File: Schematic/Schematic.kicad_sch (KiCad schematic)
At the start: 2 parts, among them U1 NRF52840-DONGLE

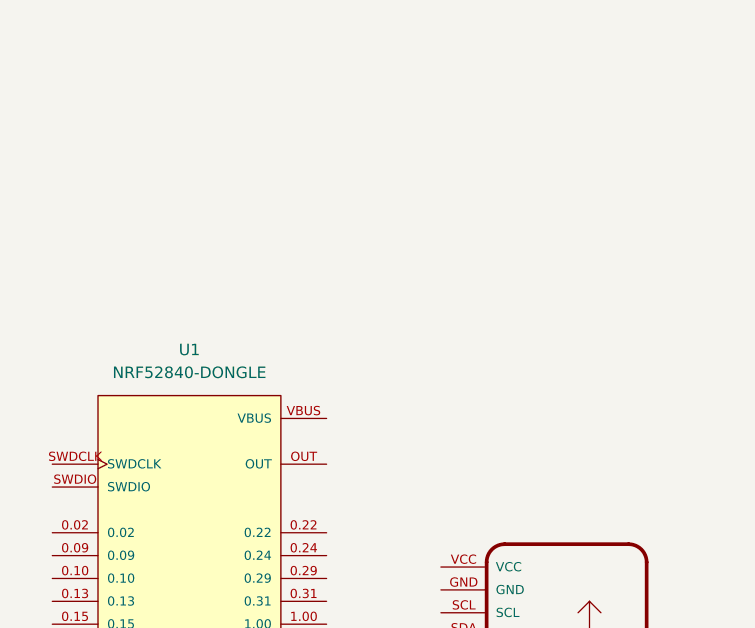
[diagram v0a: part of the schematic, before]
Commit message: PCB: adding the required symbols, footprints and 3D models
- create generic paths to the symbos and footprints, so there is no problem with setup on the other machine
- adding further PCB elements of the project
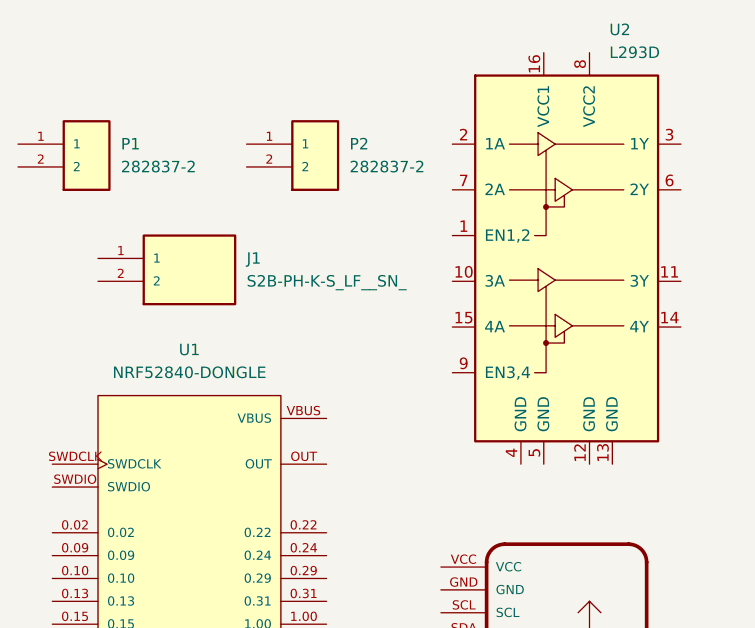
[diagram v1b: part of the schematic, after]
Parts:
- added J1: S2B-PH-K-S_LF__SN_, S2B-PH-K-S_LF__SN_:JST_S2B-PH-K-S_LF__SN_, symbol S2B-PH-K-S_LF__SN_:S2B-PH-K-S_LF__SN_
- added P1, P2: 282837-2, 282837-2:TE_282837-2, symbol 282837-2:282837-2
- added U2: L293D, Package_DIP:DIP-16_W7.62mm, symbol Driver_Motor:L293D
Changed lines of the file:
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@@
+    )
+  )
+  (symbol (lib_id "282837-2:282837-2") (at 64.77 27.94 0) (unit 1)
+    (in_bom yes) (on_board yes) (dnp no) (fields_autoplaced)
+    (property "Reference" "P1" (at 68.58 27.94 0)
+      (effects (font (size 1.27 1.27)) (justify left))
+    )
+    (property "Value" "282837-2" (at 68.58 30.48 0)
+      (effects (font (size 1.27 1.27)) (justify left))
+    )
+    (property "Footprint" "282837-2:TE_282837-2" (at 64.77 27.94 0)
+      (effects (font (size 1.27 1.27)) (justify bottom) hide)
+    )
+    (property "Datasheet" "" (at 64.77 27.94 0)
+      (effects (font (size 1.27 1.27)) hide)
+    )
+    (property "Comment" "282837-2" (at 64.77 27.94 0)
+      (effects (font (size 1.27 1.27)) (justify bottom) hide)
+    )
+    (property "MF" "TE Connectivity" (at 64.77 27.94 0)
+      (effects (font (size 1.27 1.27)) (justify bottom) hide)
+    )
+    (property "DESCRIPTION" "TERMINAL BLOCK 3.5MM 2POS PCB" (at 64.77 27.94 0)
+      (effects (font (size 1.27 1.27)) (justify bottom) hide)
+    )
+    (property "PACKAGE" "None" (at 64.77 27.94 0)
+      (effects (font (size 1.27 1.27)) (justify bottom) hide)
+    )
+    (property "PRICE" "0.28 USD" (at 64.77 27.94 0)
+      (effects (font (size 1.27 1.27)) (justify bottom) hide)
+    )
+    (property "Package" "None" (at 64.77 27.94 0)
+      (effects (font (size 1.27 1.27)) (justify bottom) hide)
+    )
+    (property "Check_prices" "https://www.snapeda.com/parts/282837-2/TE+Connectivity+AMP+Connectors/view-part/?ref=eda" (at 64.77 27.94 0)
+      (effects (font (size 1.27 1.27)) (justify bottom) hide)
+    )
+    (property "Price" "None" (at 64.77 27.94 0)
+      (effects (font (size 1.27 1.27)) (justify bottom) hide)
+    )
+    (property "PARTREV" "G3" (at 64.77 27.94 0)
+      (effects (font (size 1.27 1.27)) (justify bottom) hide)
+    )
+    (property "SnapEDA_Link" "https://www.snapeda.com/parts/282837-2/TE+Connectivity+AMP+Connectors/view-part/?ref=snap" (at 64.77 27.94 0)
+      (effects (font (size 1.27 1.27)) (justify bottom) hide)
+    )
+    (property "MP" "282837-2" (at 64.77 27.94 0)
+      (effects (font (size 1.27 1.27)) (justify bottom) hide)
+    )
+    (property "Availability" "In Stock" (at 64.77 27.94 0)
+      (effects (font (size 1.27 1.27)) (justify bottom) hide)
+    )
+    (property "AVAILABILITY" "Good" (at 64.77 27.94 0)
+      (effects (font (size 1.27 1.27)) (justify bottom) hide)
+    )
+    (property "Description" "\n                        \n                            Terminal Block Connector Wire Receptacle 2 5.08 mm 30-16 AWG Green 13.5 A 250 V | TE Connectivity 282837-2\n                        \n" (at 64.77 27.94 0)
+      (effects (font (size 1.27 1.27)) (justify bottom) hide)
+    )
+    (pin "1")
+    (pin "2")
+    (instances
+      (project "Schematic"
+        (path "/edaf4bf1-33da-445b-a3ec-56bae6383f3d"
+          (reference "P1") (unit 1)
+        )
+      )
+    )
+  )
+  (symbol (lib_id "S2B-PH-K-S_LF__SN_:S2B-PH-K-S_LF__SN_") (at 76.2 40.64 0) (unit 1)
+    (in_bom yes) (on_board yes) (dnp no) (fields_autoplaced)
+    (property "Reference" "J1" (at 82.55 40.64 0)
+      (effects (font (size 1.27 1.27)) (justify left))
+    )
+    (property "Value" "S2B-PH-K-S_LF__SN_" (at 82.55 43.18 0)
+      (effects (font (size 1.27 1.27)) (justify left))
+    )
+    (property "Footprint" "S2B-PH-K-S_LF__SN_:JST_S2B-PH-K-S_LF__SN_" (at 76.2 40.64 0)
+      (effects (font (size 1.27 1.27)) (justify bottom) hide)
+    )
+    (property "Datasheet" "" (at 76.2 40.64 0)
+      (effects (font (size 1.27 1.27)) hide)
+    )
+    (property "MF" "JST Sales America Inc." (at 76.2 40.64 0)
+      (effects (font (size 1.27 1.27)) (justify bottom) hide)
+    )
+    (property "MAXIMUM_PACKAGE_HEIGHT" "4.8mm" (at 76.2 40.64 0)
+      (effects (font (size 1.27 1.27)) (justify bottom) hide)
+    )
+    (property "PACKAGE" "None" (at 76.2 40.64 0)
+      (effects (font (size 1.27 1.27)) (justify bottom) hide)
+    )
+    (property "PRICE" "None" (at 76.2 40.64 0)
+      (effects (font (size 1.27 1.27)) (justify bottom) hide)
+    )
+    (property "Package" "NON STANDARD-2 J.S.T." (at 76.2 40.64 0)
+      (effects (font (size 1.27 1.27)) (justify bottom) hide)
+    )
+    (property "Check_prices" "https://www.snapeda.com/parts/S2B-PH-K-S(LF)(SN)/JST/view-part/?ref=eda" (at 76.2 40.64 0)
+      (effects (font (size 1.27 1.27)) (justify bottom) hide)
+    )
+    (property "Price" "None" (at 76.2 40.64 0)
+      (effects (font (size 1.27 1.27)) (justify bottom) hide)
+    )
+    (property "SnapEDA_Link" "https://www.snapeda.com/parts/S2B-PH-K-S(LF)(SN)/JST/view-part/?ref=snap" (at 76.2 40.64 0)
+      (effects (font (size 1.27 1.27)) (justify bottom) hide)
+    )
+    (property "MP" "S2B-PH-K-S(LF)(SN)" (at 76.2 40.64 0)
+      (effects (font (size 1.27 1.27)) (justify bottom) hide)
+    )
+    (property "Description" "\n                        \n                            Connector Header Through Hole, Right Angle 2 position\n                        \n" (at 76.2 40.64 0)
+      (effects (font (size 1.27 1.27)) (justify bottom) hide)
+    )
+    (property "Availability" "In Stock" (at 76.2 40.64 0)
+      (effects (font (size 1.27 1.27)) (justify bottom) hide)
+    )
+    (property "AVAILABILITY" "Unavailable" (at 76.2 40.64 0)
+      (effects (font (size 1.27 1.27)) (justify bottom) hide)
+    )
+    (property "DESCRIPTION" "Connector Header Through Hole, Right Angle 2 position" (at 76.2 40.64 0)
+      (effects (font (size 1.27 1.27)) (justify bottom) hide)
+    )
+    (pin "1")
+    (pin "2")
+    (instances
+      (project "Schematic"
+        (path "/edaf4bf1-33da-445b-a3ec-56bae6383f3d"
+          (reference "J1") (unit 1)
+        )
+      )
+    )
+  )
+  (symbol (lib_id "282837-2:282837-2") (at 90.17 27.94 0) (unit 1)
+    (in_bom yes) (on_board yes) (dnp no) (fields_autoplaced)
+    (property "Reference" "P2" (at 93.98 27.94 0)
+      (effects (font (size 1.27 1.27)) (justify left))
+    )
+    (property "Value" "282837-2" (at 93.98 30.48 0)
+      (effects (font (size 1.27 1.27)) (justify left))
+    )
+    (property "Footprint" "282837-2:TE_282837-2" (at 90.17 27.94 0)
+      (effects (font (size 1.27 1.27)) (justify bottom) hide)
+    )
+    (property "Datasheet" "" (at 90.17 27.94 0)
+      (effects (font (size 1.27 1.27)) hide)
+    )
+    (property "Comment" "282837-2" (at 90.17 27.94 0)
+      (effects (font (size 1.27 1.27)) (justify bottom) hide)
+    )
+    (property "MF" "TE Connectivity" (at 90.17 27.94 0)
+      (effects (font (size 1.27 1.27)) (justify bottom) hide)
+    )
+    (property "DESCRIPTION" "TERMINAL BLOCK 3.5MM 2POS PCB" (at 90.17 27.94 0)
+      (effects (font (size 1.27 1.27)) (justify bottom) hide)
+    )
+    (property "PACKAGE" "None" (at 90.17 27.94 0)
+      (effects (font (size 1.27 1.27)) (justify bottom) hide)
+    )
+    (property "PRICE" "0.28 USD" (at 90.17 27.94 0)
+      (effects (font (size 1.27 1.27)) (justify bottom) hide)
+    )
+    (property "Package" "None" (at 90.17 27.94 0)
+      (effects (font (size 1.27 1.27)) (justify bottom) hide)
+    )
+    (property "Check_prices" "https://www.snapeda.com/parts/282837-2/TE+Connectivity+AMP+Connectors/view-part/?ref=eda" (at 90.17 27.94 0)
+      (effects (font (size 1.27 1.27)) (justify bottom) hide)
+    )
+    (property "Price" "None" (at 90.17 27.94 0)
+      (effects (font (size 1.27 1.27)) (justify bottom) hide)
+    )
+    (property "PARTREV" "G3" (at 90.17 27.94 0)
+      (effects (font (size 1.27 1.27)) (justify bottom) hide)
+    )
+    (property "SnapEDA_Link" "https://www.snapeda.com/parts/282837-2/TE+Connectivity+AMP+Connectors/view-part/?ref=snap" (at 90.17 27.94 0)
+      (effects (font (size 1.27 1.27)) (justify bottom) hide)
+    )
+    (property "MP" "282837-2" (at 90.17 27.94 0)
+      (effects (font (size 1.27 1.27)) (justify bottom) hide)
+    )
+    (property "Availability" "In Stock" (at 90.17 27.94 0)
+      (effects (font (size 1.27 1.27)) (justify bottom) hide)
+    )
+    (property "AVAILABILITY" "Good" (at 90.17 27.94 0)
+      (effects (font (size 1.27 1.27)) (justify bottom) hide)
+    )
+    (property "Description" "\n                        \n                            Terminal Block Connector Wire Receptacle 2 5.08 mm 30-16 AWG Green 13.5 A 250 V | TE Connectivity 282837-2\n                        \n" (at 90.17 27.94 0)
+      (effects (font (size 1.27 1.27)) (justify bottom) hide)
+    )
+    (pin "1")
+    (pin "2")
+    (instances
+      (project "Schematic"
+        (path "/edaf4bf1-33da-445b-a3ec-56bae6383f3d"
+          (reference "P2") (unit 1)
+        )
+      )
     )
   )
@@
         )
       )
+    )
+  )
+  (symbol (lib_id "Driver_Motor:L293D") (at 118.11 43.18 0) (unit 1)
+    (in_bom yes) (on_board yes) (dnp no) (fields_autoplaced)
+    (property "Reference" "U2" (at 122.8441 15.24 0)
+      (effects (font (size 1.27 1.27)) (justify left))
+    )
+    (property "Value" "L293D" (at 122.8441 17.78 0)
+      (effects (font (size 1.27 1.27)) (justify left))
+    )
+    (property "Footprint" "Package_DIP:DIP-16_W7.62mm" (at 124.46 62.23 0)
+      (effects (font (size 1.27 1.27)) (justify left) hide)
+    )
+    (property "Datasheet" "http://www.ti.com/lit/ds/symlink/l293.pdf" (at 110.49 25.4 0)
+      (effects (font (size 1.27 1.27)) hide)
+    )
+    (pin "5")
+    (pin "3")
+    (pin "7")
+    (pin "6")
+    (pin "12")
+    (pin "11")
+    (pin "13")
+    (pin "14")
+    (pin "15")
+    (pin "10")
+    (pin "8")
+    (pin "16")
+    (pin "1")
+    (pin "4")
+    (pin "9")
+    (pin "2")
+    (instances
+      (project "Schematic"
+        (path "/edaf4bf1-33da-445b-a3ec-56bae6383f3d"
+          (reference "U2") (unit 1)
+        )
+      )

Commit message: PCB: Added all neecesseary symbols, footprints and 3d models
-create an demo PCB
-create 3dvis folder with apperance of the boards
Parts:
- added C1, C2, C3: 100uF, Capacitor_THT:C_Disc_D7.5mm_W4.4mm_P5.00mm, symbol Device:C
- added R1, R2, R3: 100R, Resistor_THT:R_Axial_DIN0207_L6.3mm_D2.5mm_P5.08mm_Vertical, symbol Device:R
- added S1: 1101M2S3CQE2, 1101M2S3CQE2:SW_1101M2S3CQE2, symbol 1101M2S3CQE2:1101M2S3CQE2
- added U3: LM1117DT-3.3, Package_TO_SOT_SMD:TO-252-3_TabPin2, symbol Regulator_Linear:LM1117DT-3.3
- added U4: YAAJ_DCDC_StepDown_LM2596, lm256:YAAJ_DCDC_StepDown_LM2596, symbol yaaj_dcdc_stepdown_lm2596:YAAJ_DCDC_StepDown_LM2596

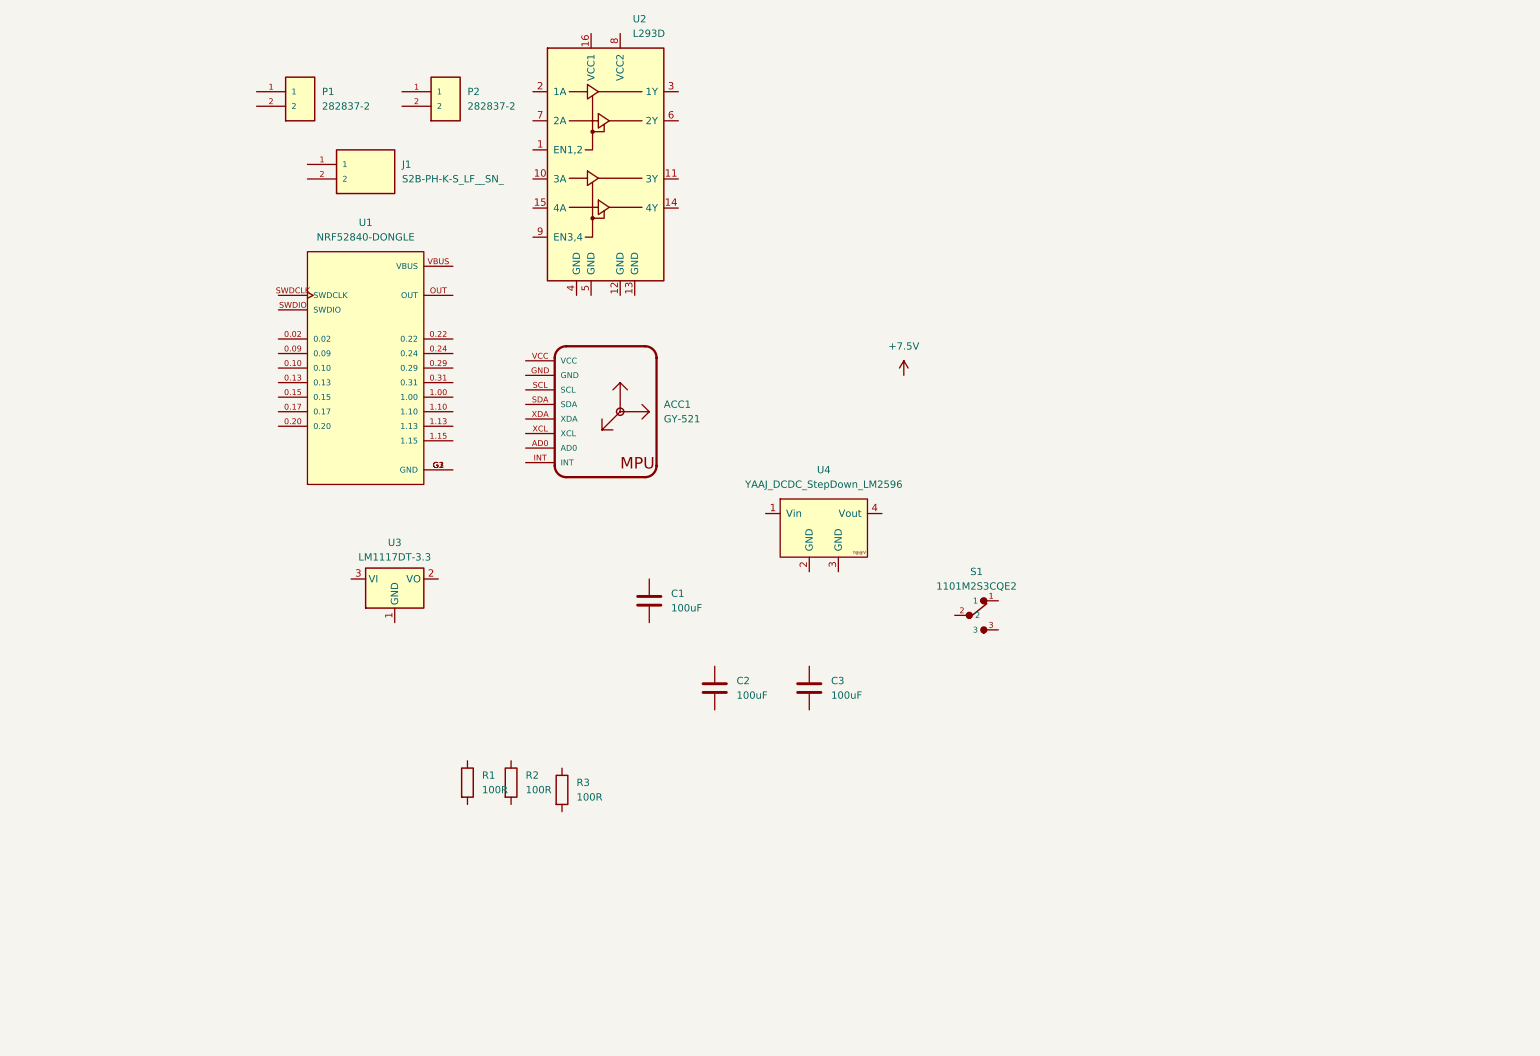
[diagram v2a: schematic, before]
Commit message: PCB: Basic schematic.
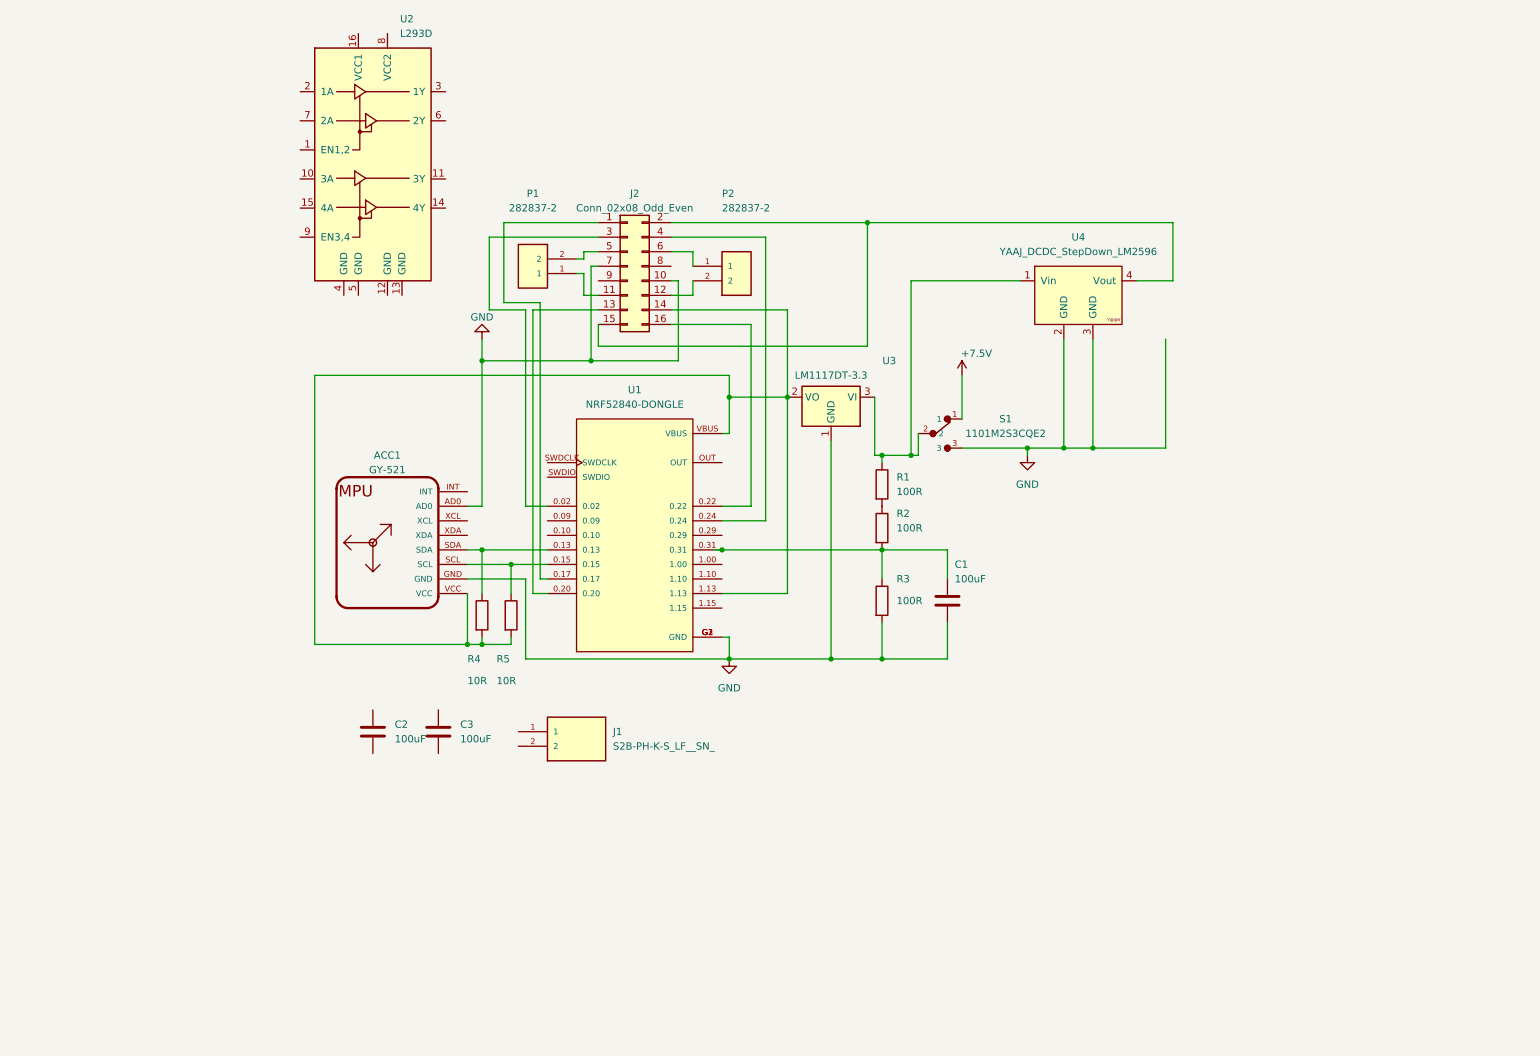
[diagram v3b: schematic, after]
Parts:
- added J2: Conn_02x08_Odd_Even, Package_DIP:DIP-16_W10.16mm, symbol Connector_Generic:Conn_02x08_Odd_Even
- added R4, R5: 10R, Resistor_THT:R_Axial_DIN0207_L6.3mm_D2.5mm_P5.08mm_Vertical, symbol Device:R
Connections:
- net +7.5V: now also S1.1
- net at U1.0.02: now also J2.3 (Pin_3)
- net at U1.0.13: now also ACC1.SDA, R4.1
- net at U1.0.15: now also ACC1.SCL, R5.1
- net at U1.0.17: now also J2.1 (Pin_1)
- net at U1.0.20: now also J2.13 (Pin_13)
- net at U1.0.22: now also J2.16 (Pin_16)
- net at U1.0.24: now also J2.4 (Pin_4)
- net at U1.0.31: now also C1.1, R2.2, R3.1
- net at U1.1.13: now also ACC1.VCC, U1.VBUS, U3.2 (VO), J2.14 (Pin_14), R4.2, R5.2
- net GND: now reaches U1.G1 (GND), U1.G2 (GND), U1.G3 (GND)
- net GND: now also ACC1.AD0, ACC1.GND, C1.2, R3.2, S1.3, U3.1 (GND), U4.2 (GND), U4.3 (GND), J2.10 (Pin_10), J2.7 (Pin_7)
- net at P1.1: now also J2.11 (Pin_11)
- net at P1.2: now also J2.5 (Pin_5)
- net at P2.1: now also J2.6 (Pin_6)
- net at P2.2: now also J2.12 (Pin_12)
- net at U4.1 (Vin): now also R1.1, S1.2, U3.3 (VI)
- net at U4.4 (Vout): now also J2.15 (Pin_15), J2.2 (Pin_2)
- net at R2.1: now also R1.2
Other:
- moved on the sheet: ACC1, C1, C2, C3, J1, P1, P2, R1, R2, R3, S1, U1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

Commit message: PCB: Basic schematic - fixes.
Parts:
- R4, R5: value 10R -> 4,7R
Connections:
- net +7.5V is gone; now on an unnamed net: S1.1
- net GND: now also J1.2, J2.8 (Pin_8), J2.9 (Pin_9)
- net at ACC1.VCC, R4.2, R5.2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: no longer J2.14 (Pin_14), U1.1.13
- net at J2.15 (Pin_15), U4.4 (Vout): no longer J2.2 (Pin_2)
- new net: J2.14 (Pin_14), U1.1.13
- new net +5V: J2.2 (Pin_2)
- no-connect marks 0 -> 3
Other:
- moved on the sheet: C2, C3, J1, U2, U4
